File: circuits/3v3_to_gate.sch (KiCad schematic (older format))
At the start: 17 parts, among them U1 LM324

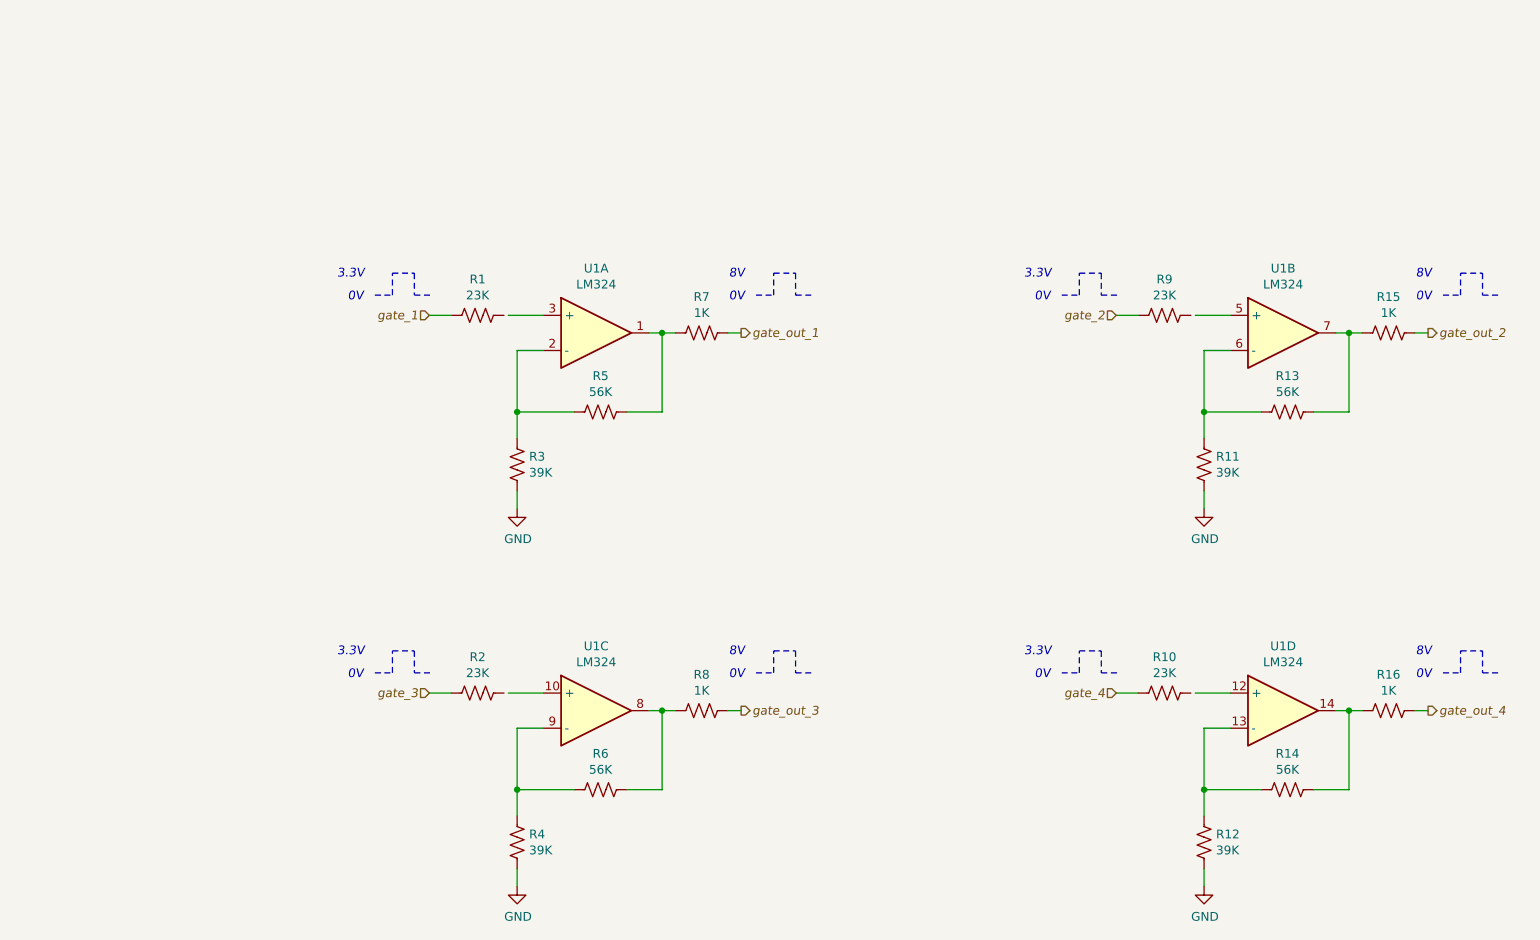
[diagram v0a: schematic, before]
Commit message: updating circuit fragements with simulation links and fixing bugs
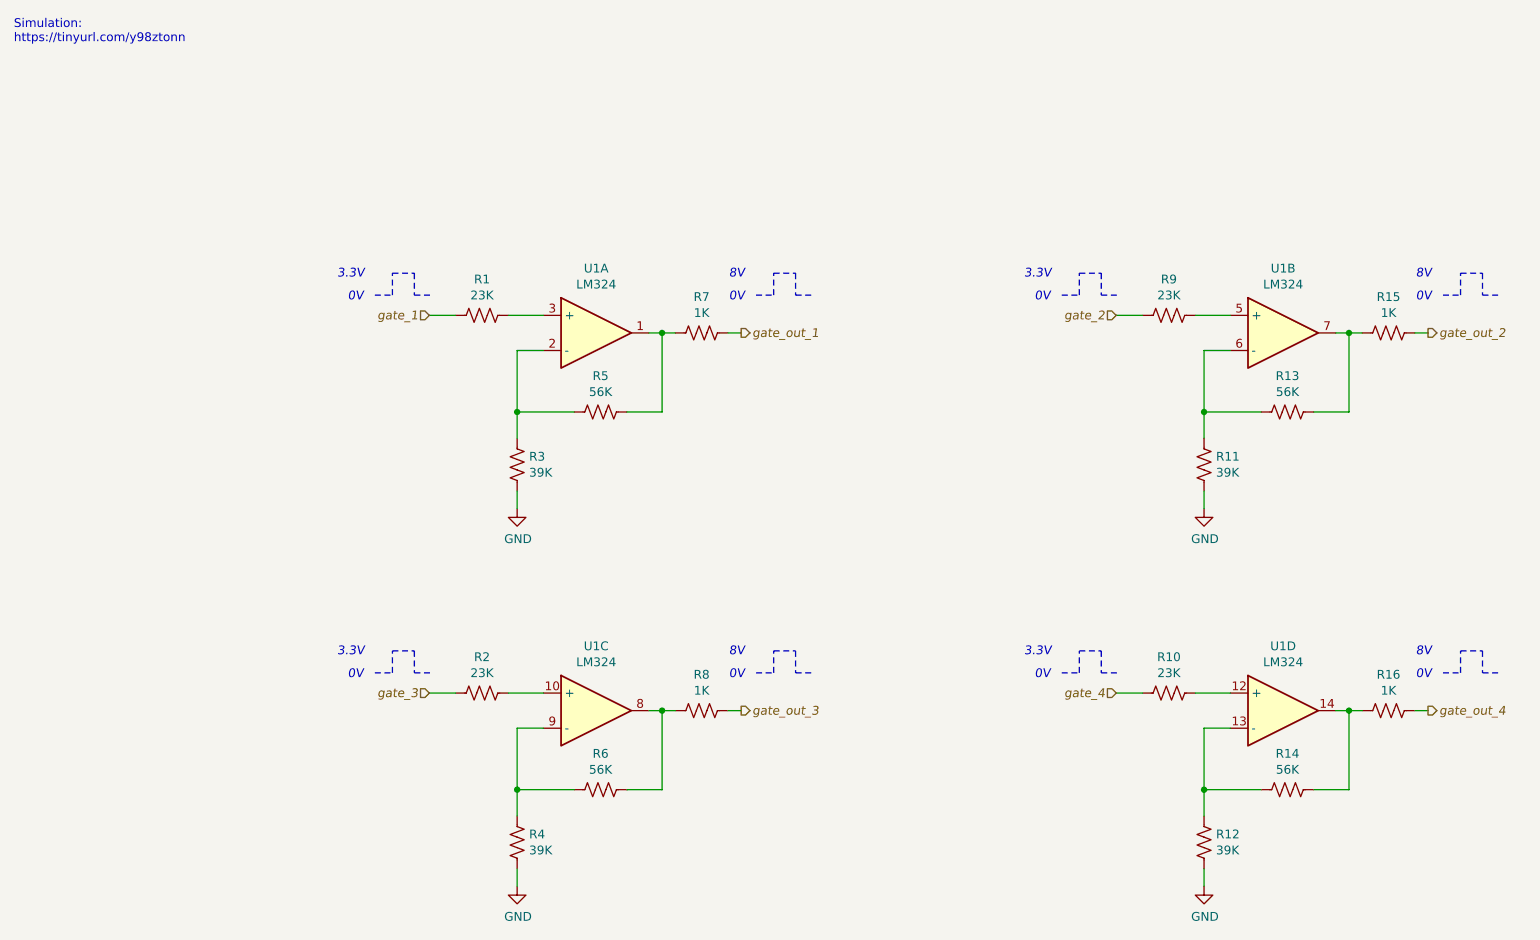
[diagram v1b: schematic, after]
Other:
- note added: "Simulation:\nhttps://tinyurl.com/y98ztonn"
- moved on the sheet: R1, R10, R2, R9
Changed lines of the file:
@@
 L Device:R_US R1
 U 1 1 62507007
-P 3290 2495
-F 0 "R1" V 3085 2495 50  0000 C CNN
-F 1 "23K" V 3176 2495 50  0000 C CNN
-F 2 "" V 3330 2485 50  0001 C CNN
-F 3 "~" H 3290 2495 50  0001 C CNN
-	1    3290 2495
+P 3315 2495
+F 0 "R1" V 3110 2495 50  0000 C CNN
+F 1 "23K" V 3201 2495 50  0000 C CNN
+F 2 "" V 3355 2485 50  0001 C CNN
+F 3 "~" H 3315 2495 50  0001 C CNN
+	1    3315 2495
 	0    1    1    0
 $EndComp
@@
 	3515 3495 3515 3595
 Wire Wire Line
-	3140 2495 3015 2495
+	3165 2495 3015 2495
 Wire Wire Line
 	4715 2595 4790 2595
@@
 L Device:R_US R2
 U 1 1 6251FB31
-P 3290 4645
-F 0 "R2" V 3085 4645 50  0000 C CNN
-F 1 "23K" V 3176 4645 50  0000 C CNN
-F 2 "" V 3330 4635 50  0001 C CNN
-F 3 "~" H 3290 4645 50  0001 C CNN
-	1    3290 4645
+P 3315 4645
+F 0 "R2" V 3110 4645 50  0000 C CNN
+F 1 "23K" V 3201 4645 50  0000 C CNN
+F 2 "" V 3355 4635 50  0001 C CNN
+F 3 "~" H 3315 4645 50  0001 C CNN
+	1    3315 4645
 	0    1    1    0
 $EndComp
@@
 	3515 5645 3515 5745
 Wire Wire Line
-	3140 4645 3015 4645
+	3165 4645 3015 4645
 Wire Wire Line
 	4715 4745 4790 4745
@@
 L Device:R_US R9
 U 1 1 6252247F
-P 7200 2495
-F 0 "R9" V 6995 2495 50  0000 C CNN
-F 1 "23K" V 7086 2495 50  0000 C CNN
-F 2 "" V 7240 2485 50  0001 C CNN
-F 3 "~" H 7200 2495 50  0001 C CNN
-	1    7200 2495
+P 7225 2495
+F 0 "R9" V 7020 2495 50  0000 C CNN
+F 1 "23K" V 7111 2495 50  0000 C CNN
+F 2 "" V 7265 2485 50  0001 C CNN
+F 3 "~" H 7225 2495 50  0001 C CNN
+	1    7225 2495
 	0    1    1    0
 $EndComp
@@
 	7425 3495 7425 3595
 Wire Wire Line
-	7050 2495 6925 2495
+	7075 2495 6925 2495
 Wire Wire Line
 	8625 2595 8700 2595
@@
 L Device:R_US R10
 U 1 1 62526018
-P 7200 4645
-F 0 "R10" V 6995 4645 50  0000 C CNN
-F 1 "23K" V 7086 4645 50  0000 C CNN
-F 2 "" V 7240 4635 50  0001 C CNN
-F 3 "~" H 7200 4645 50  0001 C CNN
-	1    7200 4645
+P 7225 4645
+F 0 "R10" V 7020 4645 50  0000 C CNN
+F 1 "23K" V 7111 4645 50  0000 C CNN
+F 2 "" V 7265 4635 50  0001 C CNN
+F 3 "~" H 7225 4645 50  0001 C CNN
+	1    7225 4645
 	0    1    1    0
 $EndComp
@@
 	7425 5645 7425 5745
 Wire Wire Line
-	7050 4645 6925 4645
+	7075 4645 6925 4645
 Wire Wire Line
 	8625 4745 8700 4745
@@
 EndData
 $EndBitmap
+Text Notes 650  950  0    50   ~ 0
+Simulation:\nhttps://tinyurl.com/y98ztonn
 $EndSCHEMATC
